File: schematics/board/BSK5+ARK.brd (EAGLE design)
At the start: 94 x 94 mm, 88 parts, among them U1 STM32F405RGT6, X1 JST-6A, X11 JST-6A

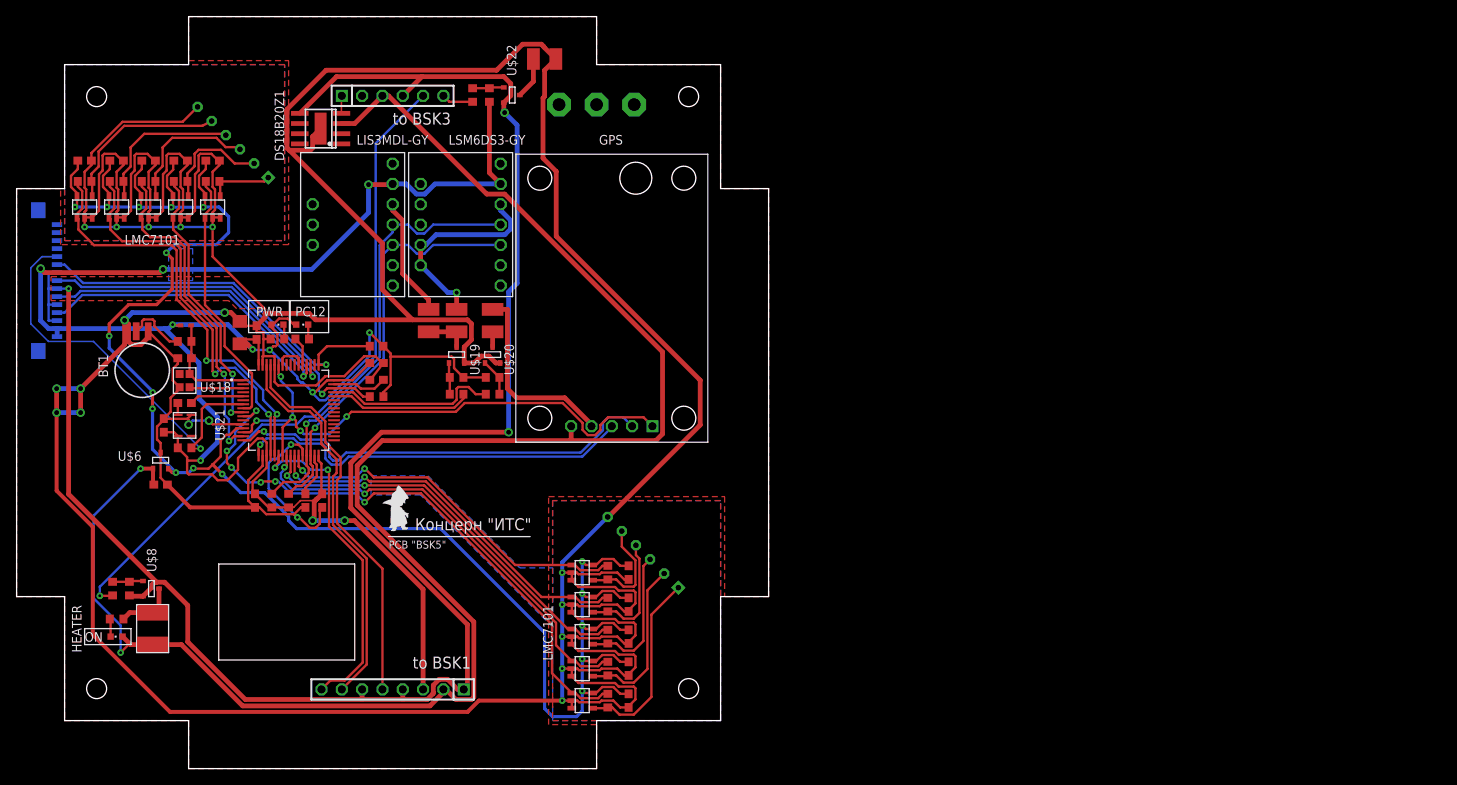
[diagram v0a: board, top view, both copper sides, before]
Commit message: Завершена разработка плат БСК5 и АРК, половина платы БКУ разведена, добавлены гербер файлы плат АРК, БСК5 и WSPR
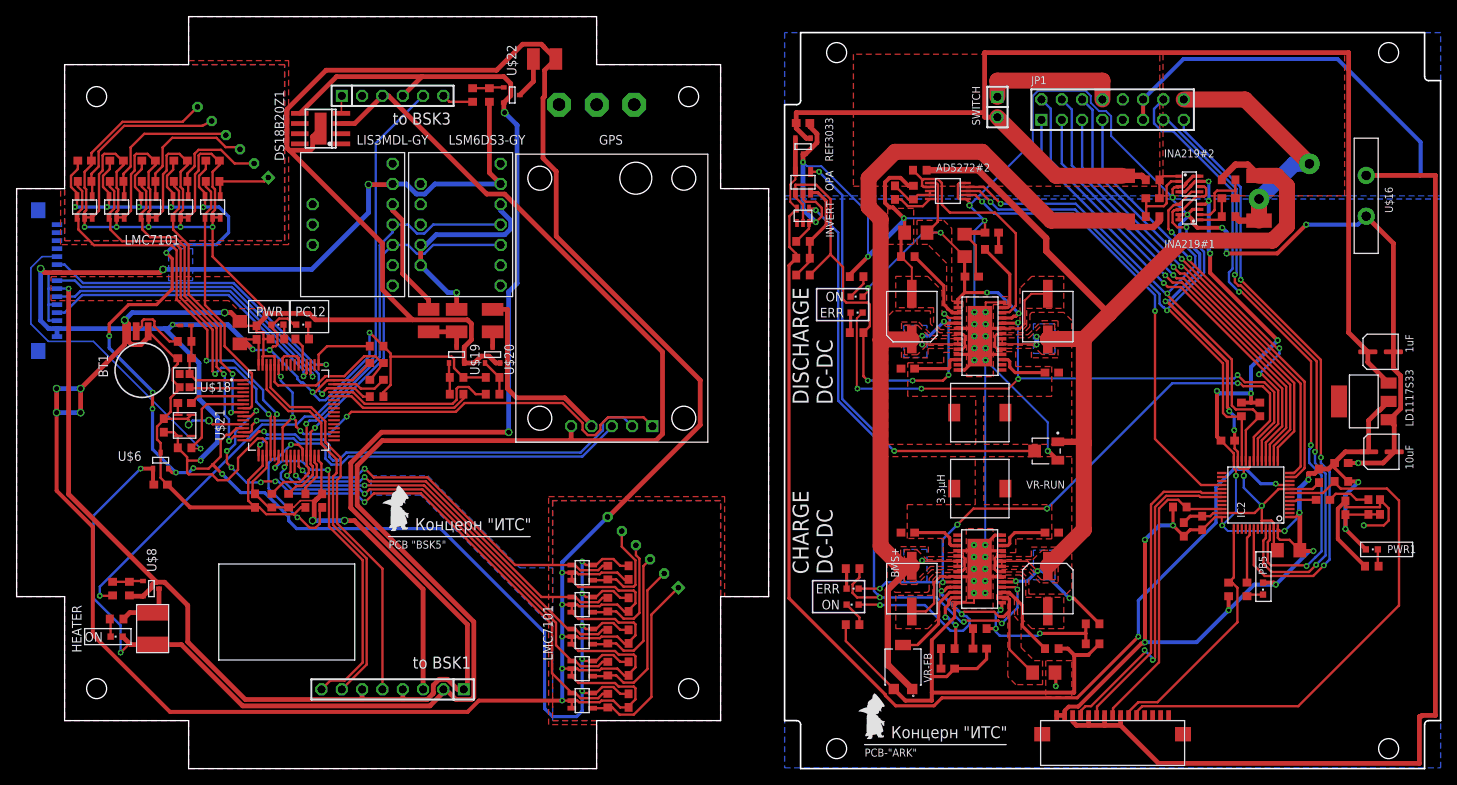
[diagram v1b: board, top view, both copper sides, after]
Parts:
- added 3,3µH: 3,3µ, CanCubeSat:B82472G6
- added 3,3µH1: 3,3µH, CanCubeSat:B82472G6
- added AD5272#2: AD5272, CanCubeSat:MSOP10
- added C10, C47: 150µ, CanCubeSat:ECAP150-CMD
- added C21, C48: 220µ, CanCubeSat:ECAP220-CMD
- added C22, C23, C25, C26, C27: 100nF, rcl:C0603
- added C24, C57: 10µ, rcl:C1206
- added C28, C29, C40, C41, C49, C50, C56: 0,1µ, rcl:C0603
- added C30: 1nF, rcl:C0603
- added C31: 10nF, rcl:C0603
- added C32: 1µ, rcl:C0603
- added C33: 470nF, rcl:C0603
- added C34: 10uF, CanCubeSat:ECAP-SMD-D4
- added C35: 1uF, CanCubeSat:ECAP-SMD-D4
- added C44, C52: 680p, rcl:C0603
- added C45, C53: 4.7µ, rcl:C1206
- added C46: 3,3n, rcl:C0603
- added IC2: STM32F103C8T, CanCubeSat:LQFP48
- added INA219#1, INA219#2: INA219AID, CanCubeSat:SOT23-8
- added INVERT: INVERTER., CanCubeSat:SC70
- added JP1: (no value), pinheadCS:2X08
- added LD1117S33: LD1117S33, CanCubeSat:SOT223
- added LED_G1, LED_G2, LED_R1, LED_R2, PB5, PWR1: (no value), led:CHIPLED_0603
- added OPA: OPA333, CanCubeSat:SOT23-5
- added R100, R27, R35, R57, R81, R82: 2k, resistor:R0603
- added R101, R102: 5k1, resistor:R0603
- added R11, R17, R67, R68, R69: 150k, resistor:R0603
- added R36, R64, R66, R79: 10k, resistor:R0603
- added R37: 14K3, resistor:R0603
- added R38: 91K, resistor:R0603
- added R39: 430k, resistor:R0603
- added R40: 680k, resistor:R0603
- added R41: 120k, resistor:R0603
- added R65: 1M, resistor:R0603
- added R71, R75: R01, rcl:R2512
- added R73, R74, R76, R77: 10R, resistor:R0603
- added REF3033: REF3033, CanCubeSat:SOT23-3
- added SWITCH: (no value), pinheadCS:1X02
- added TCXO: OC2E08000XCCDRX, CanCubeSat:OC2E08000XCCDRX
- added U$14, U$59: LTC31191, CanCubeSat:LTC3119+VIA
- added U$15: FFC-CONNECT68611, CanCubeSat:68611
- added U$16: MF-R400, CanCubeSat:MF-R400
- added U$17, U$24: PCB-"ARK", CanCubeSat:ITS-LOGO
- added VR-FB: 3314G-1-504E, CanCubeSat:TRIM_3314G-1-504E
- added VR-RUN: 3313J-1-205E, CanCubeSat:TRIM_3313J-1-205E
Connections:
- new net 1W1: IC2.17, JP1.7
- new net 3V1: C22.1, C23.1, C24.1, C25.1, C26.1, C27.1, C31.2, C34.P+, IC2.1, IC2.24, IC2.36, IC2.48, INA219#1.4, INA219#2.4, INA219#2.7, LD1117S33.P$3, PB5.A, PWR1.A, R101.1, R102.1, R36.1, R64.1, R79.1, TCXO.P$1, TCXO.P$4, U$15.P$1, U$15.P$2
- new net 3V3-STAB1: IC2.9, INVERT.P$5, OPA.P$5, R41.1, REF3033.2
- new net 90: R65.1, R66.2, R67.2, U$59.15
- new net A: INVERT.P$2, OPA.P$1, R35.1, R40.1, U$14.18
- new net BMS+: C33.2, C35.P+, LD1117S33.P$4, R75.2, R76.1, REF3033.1, SWITCH.2
- new net BMS+_OUT: JP1.8, SWITCH.1
- new net BMS1: IC2.16, JP1.1
- new net BMS2: IC2.15, JP1.2
- new net BMS3: IC2.14, JP1.3
- new net BMS4: IC2.13, JP1.4
- new net BMS5: IC2.12, JP1.5
- new net BMS6: IC2.11, JP1.6
- new net BUS+1: JP1.16, R71.2, R73.1
- new net DPD_RST: AD5272#2.7, IC2.28
- new net GND-OUT1: JP1.11, JP1.12, U$15.P$3, U$15.P$5, U$15.P$7, U$15.P$9, U$16.P$2
- new net GND1: AD5272#2.10, AD5272#2.6, C10.P$2, C21.P$2, C22.2, C23.2, C24.2, C25.2, C26.2, C27.2, C31.1, C33.1, C34.P-, C35.P-, C44.2, C45.2, C46.2, C47.P$2, C48.P$2, C52.2, C53.2, C56.2, C57.2, IC2.20, IC2.23, IC2.35, IC2.44, IC2.47, IC2.8, INA219#1.3, INA219#1.7, INA219#1.8, INA219#2.3, INA219#2.8, INVERT.P$3, LD1117S33.P$2, OPA.P$2, R100.1, R11.1, R27.1, R37.2, R39.1, R67.1, R68.1, R82.1, REF3033.3, TCXO.P$2, U$14.14, U$14.20, U$14.25, U$14.28, U$14.29, U$14.4, U$14.9, U$14.P$1, U$14.P$10, U$14.P$2, U$14.P$3, U$14.P$4, U$14.P$5, U$14.P$6, U$14.P$7, U$14.P$8, U$14.P$9, U$16.P$1, U$59.14, U$59.20, U$59.25, U$59.28, U$59.29, U$59.4, U$59.9, U$59.P$1, U$59.P$10, U$59.P$2, U$59.P$3, U$59.P$4, U$59.P$5, U$59.P$6, U$59.P$7, U$59.P$8, U$59.P$9, VR-FB.3, VR-RUN.3
- new net INA_BMS+: C21.P$1, C47.P$1, R75.1, R77.1, U$14.19, U$14.22, U$14.23, U$59.6, U$59.7, VR-FB.1
- new net INA_BUS+: C10.P$1, C48.P$1, R38.1, R65.2, R71.1, R74.1, U$14.6, U$14.7, U$59.19, U$59.22, U$59.23, VR-RUN.1
- new net N$129: C41.2, U$59.3
- new net N$131: 3,3µH.2, C40.1, U$59.21, U$59.24
- new net N$132: 3,3µH.1, C41.1, U$59.5, U$59.8
- new net N$135: R69.1, U$59.13
- new net N$136: C44.1, R69.2
- new net N$139: C46.1, R66.1
- new net N$142: R68.2, U$59.17
- new net N$144: C40.2, U$59.26
- new net N$147: C28.1, INA219#1.1, R73.2
- new net N$15: AD5272#2.3, AD5272#2.4, C32.2, R37.1
- new net N$150: C29.1, INA219#2.1, R76.2
- new net N$151: C29.2, INA219#2.2, R77.2
- new net N$159: PWR1.C, R82.2
- new net N$16: AD5272#2.2, R38.2, U$14.12
- new net N$161: IC2.41, R81.1
- new net N$17: PB5.C, R81.2
- new net N$18: OPA.P$3, R39.2, R40.2, R41.2
- new net N$215: AD5272#2.1, C53.1, C56.1, C57.1, LED_G2.A, U$14.11, U$14.15, U$14.16
- new net N$234: C45.1, LED_G1.A, U$59.11, U$59.16
- new net N$3: C28.2, INA219#1.2, R74.2
- new net N$51: AD5272#2.5, C32.1
- new net N$77: 3,3µH1.2, C49.1, U$14.21, U$14.24
- new net N$78: 3,3µH1.1, C50.1, U$14.5, U$14.8
- new net N$79: R11.2, U$14.17
- new net N$8: C30.2, TCXO.P$3
- new net N$80: C49.2, U$14.26
- new net N$81: R17.1, U$14.13
- new net N$82: C52.1, R17.2
- new net N$84: C50.2, U$14.3
- new net N$85: LED_R1.A, R35.2
- new net N$87: LED_R2.A, R57.2
- new net N$89: U$59.12, VR-FB.2
- new net N$9: C30.1, IC2.5
- new net N$91: LED_G1.C, R100.2
- new net N$92: LED_G2.C, R27.2
- new net NRST1: IC2.7, R79.2, U$15.P$11
- new net PGOOD1: IC2.19, LED_R2.C, U$59.10
- new net PGOOD2: IC2.18, LED_R1.C, U$14.10
- new net RUN: OPA.P$4, VR-RUN.2
- new net RX-S1: IC2.31, U$15.P$4
- new net SCL1: AD5272#2.9, IC2.21, INA219#1.5, INA219#2.5, R101.2
- new net SCLTM: IC2.45, JP1.13
- new net SDA1: AD5272#2.8, IC2.22, INA219#1.6, INA219#2.6, R102.2
- new net SDATM: IC2.46, JP1.14
- new net SWC1: IC2.37, R36.2, U$15.P$10
- new net SWD1: IC2.34, R64.2, U$15.P$8
- new net TIME: IC2.42, JP1.15
- new net TX-S1: IC2.30, U$15.P$6
- new net Y: INVERT.P$4, R57.1, U$59.18
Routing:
- net GND1: track 0.00 -> 486.6 mm, vias 0 -> 20
- net 3V1: track 0.00 -> 202.4 mm, vias 0 -> 19
- net GND-OUT1: track 0.00 -> 188.6 mm
- net BMS+: track 0.00 -> 148.2 mm
- net INA_BUS+: track 0.00 -> 145.9 mm, vias 0 -> 5
- net 3V3-STAB1: track 0.00 -> 145.8 mm, vias 0 -> 2
- net INA_BMS+: track 0.00 -> 135.6 mm, vias 0 -> 4
- net Y: track 0.00 -> 83.6 mm, vias 0 -> 5
- net PGOOD2: track 0.00 -> 82.1 mm, vias 0 -> 5
- net SDA1: track 0.00 -> 79.5 mm, vias 0 -> 3
- net SDATM: track 0.00 -> 79.2 mm, vias 0 -> 3
- net TIME: track 0.00 -> 77.9 mm, vias 0 -> 3
- net SCLTM: track 0.00 -> 77.3 mm, vias 0 -> 3
- net PGOOD1: track 0.00 -> 76.9 mm, vias 0 -> 5
- net SCL1: track 0.00 -> 76.5 mm, vias 0 -> 3
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- added copper zone on layer 1, net BMS+
- added copper zone on layer 1, net BUS+1
- added copper zone on layer 16, net GND-OUT1
- added copper zone on layer 1, net GND1
- added copper zone on layer 16, net GND1
- added copper zone on layer 1, net INA_BMS+
- added copper zone on layer 16, net INA_BMS+
- added copper zone on layer 1, net INA_BUS+
- added copper zone on layer 16, net INA_BUS+
- added copper zone on layer 1, net N$131
- added copper zone on layer 1, net N$132
- added copper zone on layer 1, net N$215
- added copper zone on layer 1, net N$234
- added copper zone on layer 1, net N$77
- added copper zone on layer 1, net N$78
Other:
- board size 94 x 94 mm -> 178 x 94 mm
- board text added: "BMS+"
- board text added: "CHARGE DC-DC"
- board text added: "DISCHARGE DC-DC"
- board text added: "ERR"
